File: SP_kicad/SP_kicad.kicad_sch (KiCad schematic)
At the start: 15 parts, among them J1 NES-CART, J2 NES-CART-CONN, J3 MIDI, J4 5V_IN, SW1 BUS_PWR, SW2 CMOD_PWR, U1 CMOD-A7, U2 LD1117V33

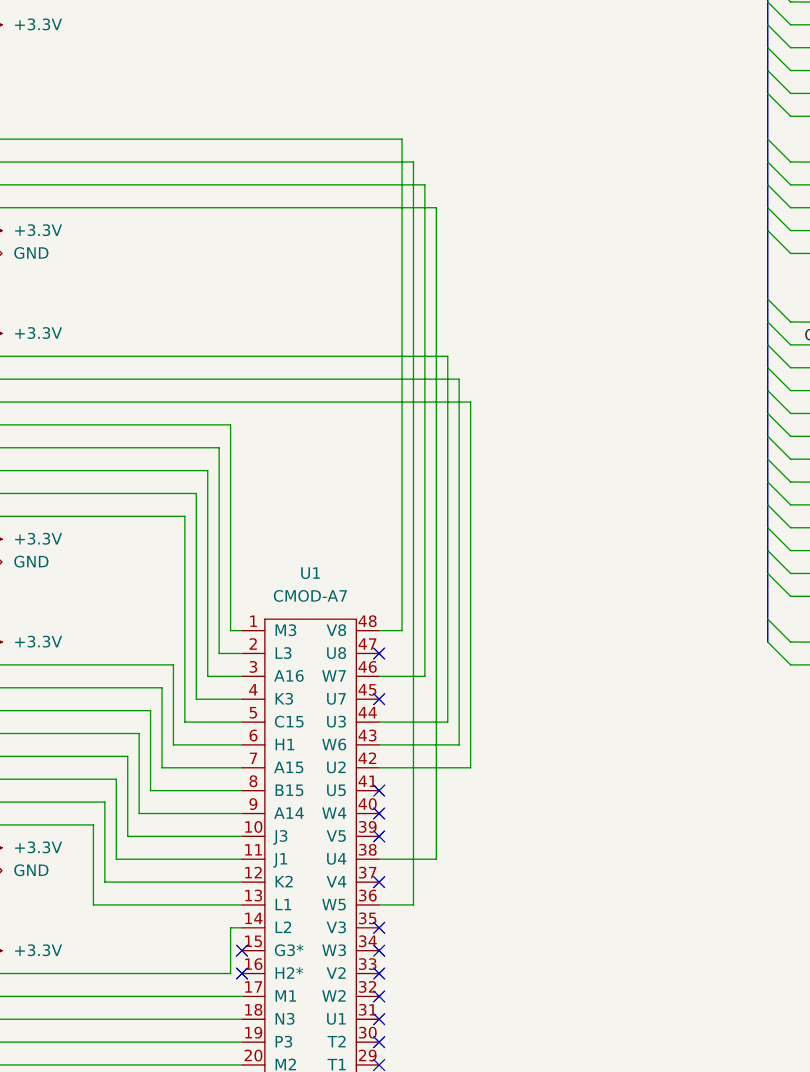
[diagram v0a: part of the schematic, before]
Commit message: Moved Kicad footprints into project
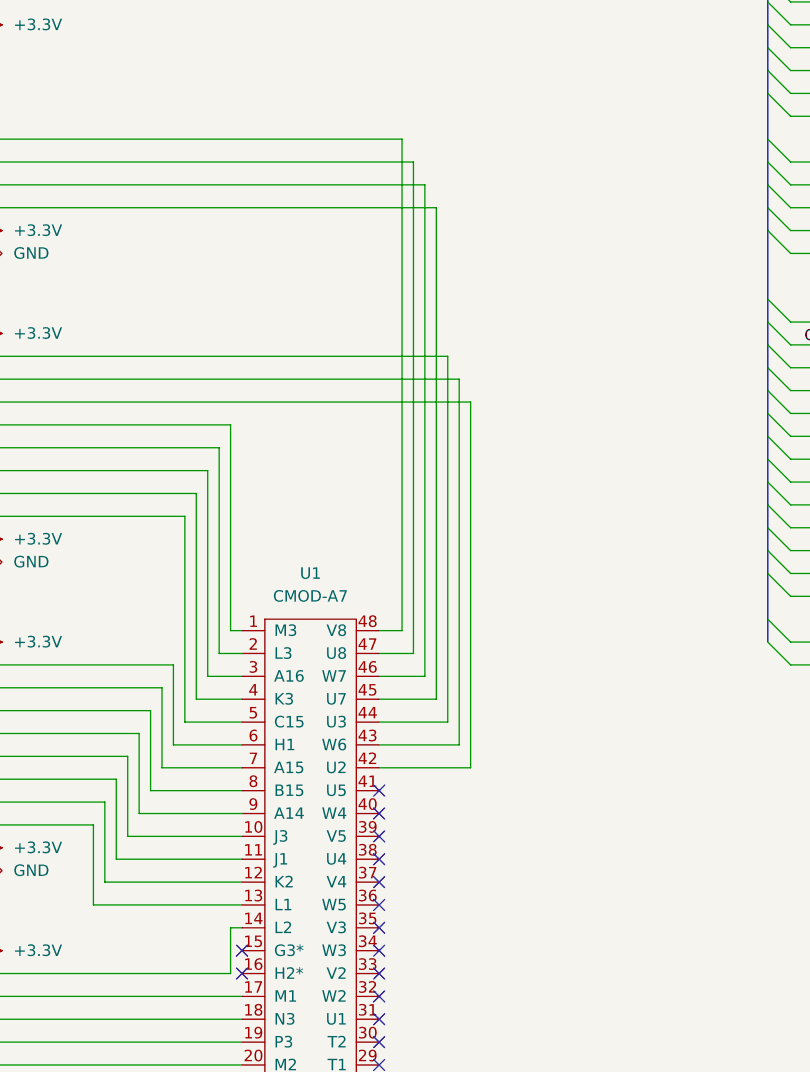
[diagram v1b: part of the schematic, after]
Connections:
- net at U1.36 (W5): no longer U6.5 (A3)
- net at U1.38 (U4): no longer U6.3 (A1)
- net at U1.45 (U7): now also U6.3 (A1)
- net at U1.47 (U8): now also U6.5 (A3)
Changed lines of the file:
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@@
   (no_connect (at 105.41 162.56))
   (no_connect (at 105.41 152.4))
-  (no_connect (at 105.41 127))
   (no_connect (at 60.96 34.29))
-  (no_connect (at 105.41 121.92))
   (no_connect (at 45.72 57.15))
   (no_connect (at 60.96 57.15))
@@
   (no_connect (at 105.41 157.48))
   (no_connect (at 105.41 170.18))
+  (no_connect (at 105.41 144.78))
   (no_connect (at 60.96 62.23))
   (no_connect (at 45.72 34.29))
@@
   (no_connect (at 105.41 165.1))
   (no_connect (at 60.96 54.61))
+  (no_connect (at 105.41 149.86))
   (no_connect (at 195.58 151.13))
   (no_connect (at 90.17 157.48))
@@
     (stroke (width 0) (type default))
   )
-  (wire (pts (xy 109.22 149.86) (xy 105.41 149.86))
-    (stroke (width 0) (type default))
-  )
   (bus (pts (xy 205.74 80.01) (xy 205.74 82.55))
     (stroke (width 0) (type default))
@@
     (stroke (width 0) (type default))
   )
+  (wire (pts (xy 111.76 127) (xy 105.41 127))
+    (stroke (width 0) (type default))
+  )
   (wire (pts (xy 80.01 137.16) (xy 90.17 137.16))
     (stroke (width 0) (type default))
@@
     (stroke (width 0) (type default))
   )
+  (wire (pts (xy 109.22 121.92) (xy 105.41 121.92))
+    (stroke (width 0) (type default))
+  )
   (bus (pts (xy 215.9 72.39) (xy 215.9 74.93))
     (stroke (width 0) (type default))
@@
     (stroke (width 0) (type default))
   )
-  (wire (pts (xy 111.76 144.78) (xy 105.41 144.78))
+  (wire (pts (xy 109.22 67.31) (xy 109.22 121.92))
     (stroke (width 0) (type default))
   )
@@
     (stroke (width 0) (type default))
   )
+  (wire (pts (xy 111.76 72.39) (xy 111.76 127))
+    (stroke (width 0) (type default))
+  )
   (wire (pts (xy 218.44 105.41) (xy 229.87 105.41))
     (stroke (width 0) (type default))
@@
     (stroke (width 0) (type default))
   )
-  (wire (pts (xy 111.76 72.39) (xy 111.76 144.78))
-    (stroke (width 0) (type default))
-  )
   (wire (pts (xy 151.13 44.45) (xy 162.56 44.45))
     (stroke (width 0) (type default))
@@
     (stroke (width 0) (type default))
   )
-  (wire (pts (xy 109.22 67.31) (xy 109.22 149.86))
-    (stroke (width 0) (type default))
-  )

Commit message: Updated M2 and SYSTEM_CLK placement
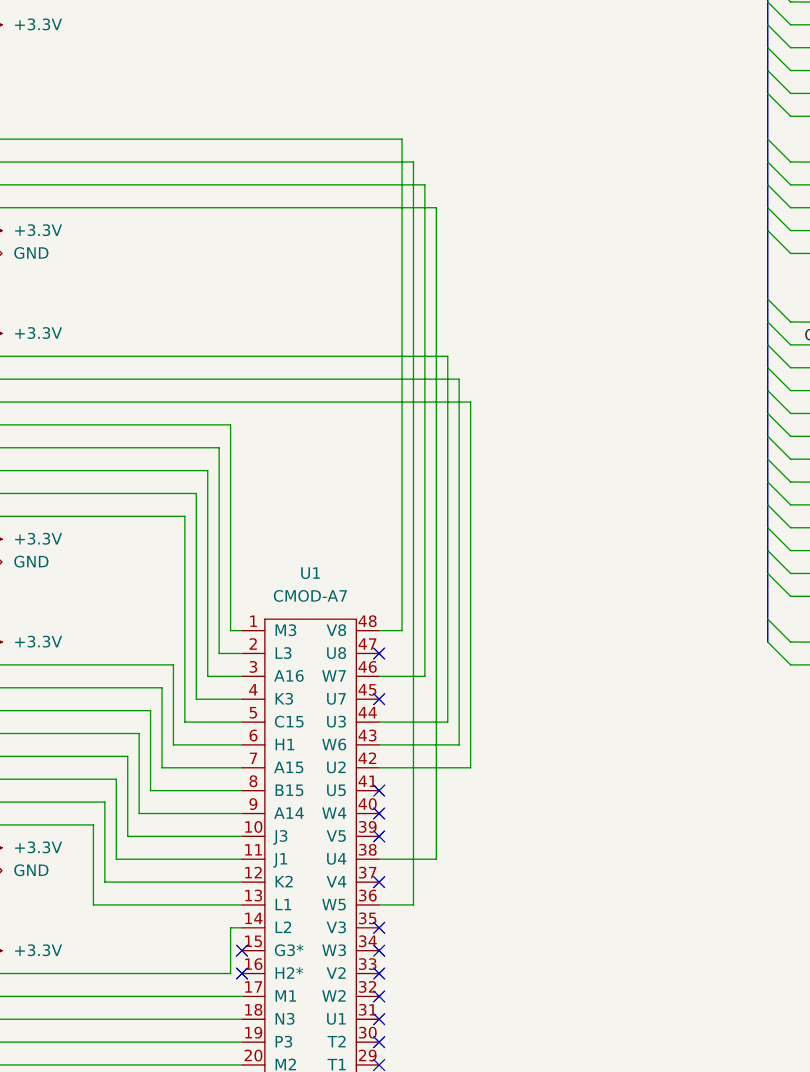
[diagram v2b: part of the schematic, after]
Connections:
- net at U1.36 (W5): now also U6.5 (A3)
- net at U1.38 (U4): now also U6.3 (A1)
- net at U1.45 (U7): no longer U6.3 (A1)
- net at U1.47 (U8): no longer U6.5 (A3)
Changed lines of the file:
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@@
   (no_connect (at 105.41 162.56))
   (no_connect (at 105.41 152.4))
+  (no_connect (at 105.41 127))
   (no_connect (at 60.96 34.29))
+  (no_connect (at 105.41 121.92))
   (no_connect (at 45.72 57.15))
   (no_connect (at 60.96 57.15))
@@
   (no_connect (at 105.41 157.48))
   (no_connect (at 105.41 170.18))
-  (no_connect (at 105.41 144.78))
   (no_connect (at 60.96 62.23))
   (no_connect (at 45.72 34.29))
@@
   (no_connect (at 105.41 165.1))
   (no_connect (at 60.96 54.61))
-  (no_connect (at 105.41 149.86))
   (no_connect (at 195.58 151.13))
   (no_connect (at 90.17 157.48))
@@
     (stroke (width 0) (type default))
   )
+  (wire (pts (xy 109.22 149.86) (xy 105.41 149.86))
+    (stroke (width 0) (type default))
+  )
   (bus (pts (xy 205.74 80.01) (xy 205.74 82.55))
     (stroke (width 0) (type default))
@@
     (stroke (width 0) (type default))
   )
-  (wire (pts (xy 111.76 127) (xy 105.41 127))
-    (stroke (width 0) (type default))
-  )
   (wire (pts (xy 80.01 137.16) (xy 90.17 137.16))
     (stroke (width 0) (type default))
@@
     (stroke (width 0) (type default))
   )
-  (wire (pts (xy 109.22 121.92) (xy 105.41 121.92))
-    (stroke (width 0) (type default))
-  )
   (bus (pts (xy 215.9 72.39) (xy 215.9 74.93))
     (stroke (width 0) (type default))
@@
     (stroke (width 0) (type default))
   )
-  (wire (pts (xy 109.22 67.31) (xy 109.22 121.92))
+  (wire (pts (xy 111.76 144.78) (xy 105.41 144.78))
     (stroke (width 0) (type default))
   )
@@
     (stroke (width 0) (type default))
   )
-  (wire (pts (xy 111.76 72.39) (xy 111.76 127))
-    (stroke (width 0) (type default))
-  )
   (wire (pts (xy 218.44 105.41) (xy 229.87 105.41))
     (stroke (width 0) (type default))
@@
     (stroke (width 0) (type default))
   )
+  (wire (pts (xy 111.76 72.39) (xy 111.76 144.78))
+    (stroke (width 0) (type default))
+  )
   (wire (pts (xy 151.13 44.45) (xy 162.56 44.45))
     (stroke (width 0) (type default))
@@
     (stroke (width 0) (type default))
   )
+  (wire (pts (xy 109.22 67.31) (xy 109.22 149.86))
+    (stroke (width 0) (type default))
+  )
